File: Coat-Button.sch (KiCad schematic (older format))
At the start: 24 parts, among them IC1 MADW__ATTINY13-MM, P1 CONN_1, P2 CONN_1, P3 CONN_1, P4 CONN_1

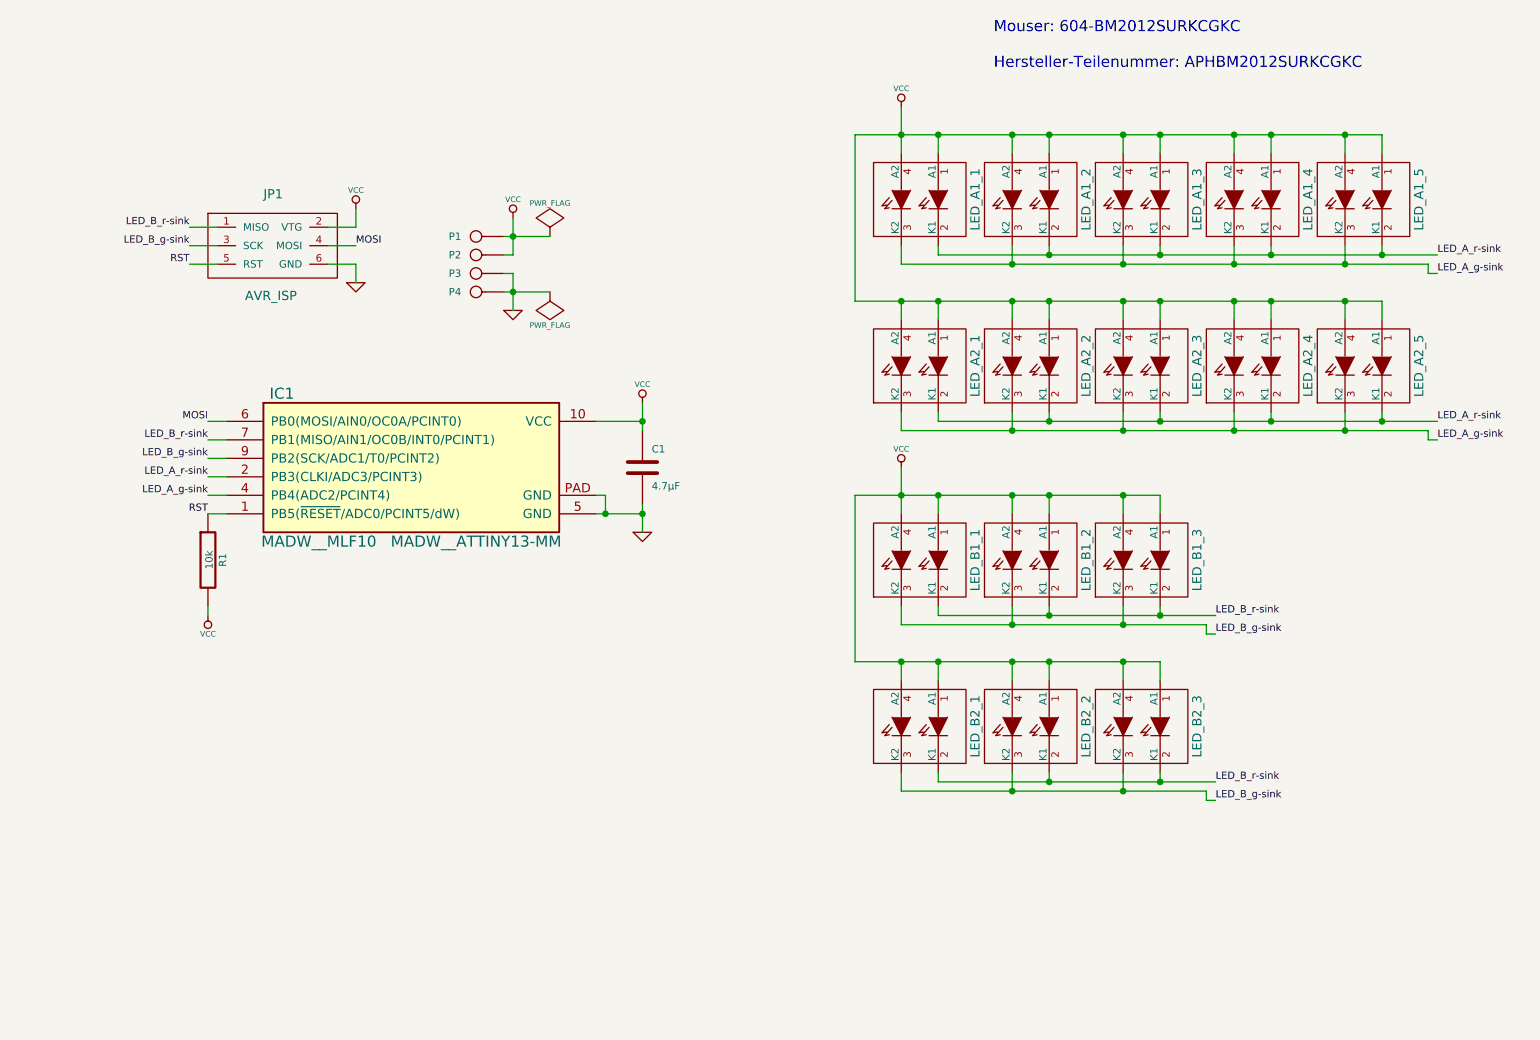
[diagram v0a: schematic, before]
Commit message: On-board ATtiny13 wasn't doable. Not enough space.
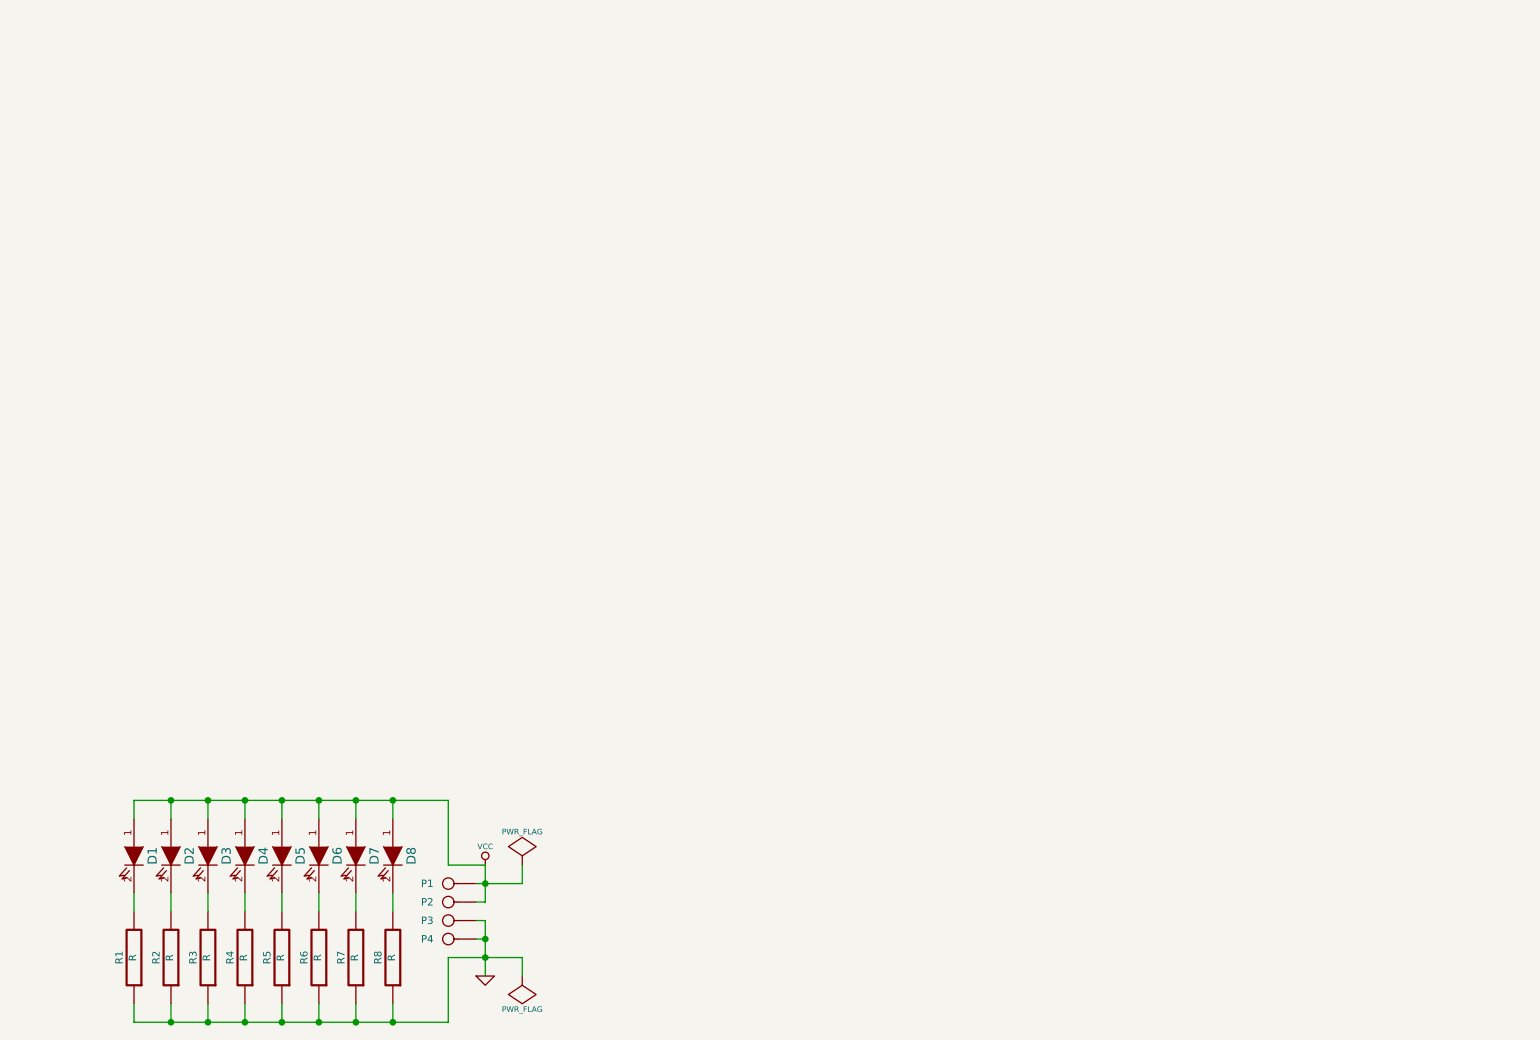
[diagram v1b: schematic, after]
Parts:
- removed C1: 4.7µF, symbol C
- removed IC1: MADW__ATTINY13-MM, MADW__MLF10, symbol MADW__ATTINY13-MM
- removed JP1: AVR_ISP, symbol MADW__AVR_ISP
- removed LED_A1_1, LED_A1_2, LED_A1_3, LED_A1_4, LED_A1_5, LED_A2_1, LED_A2_2, LED_A2_3, LED_A2_4, LED_A2_5, LED_B1_1, LED_B1_2, LED_B1_3, LED_B2_1, LED_B2_2, LED_B2_3: MADW__BI-LED, symbol MADW__BI-LED
- added D1, D2, D3, D4, D5, D6, D7, D8: LED, symbol LED
- added R2, R3, R4, R5, R6, R7, R8: R, symbol R
- R1: value 10k -> R
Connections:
- net RST is gone; now on net GND: R1.1
- net GND: now also R2.1, R3.1, R4.1, R5.1, R6.1, R7.1, R8.1
- net VCC: now also D1.1 (A), D2.1 (A), D3.1 (A), D4.1 (A), D5.1 (A), D6.1 (A), D7.1 (A), D8.1 (A); no longer R1.2
- new net: D1.2 (K), R1.2
- new net: D2.2 (K), R2.2
- new net: D3.2 (K), R3.2
- new net: D4.2 (K), R4.2
- new net: D5.2 (K), R5.2
- new net: D6.2 (K), R6.2
- new net: D7.2 (K), R7.2
- new net: D8.2 (K), R8.2
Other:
- note removed: "Mouser: 604-BM2012SURKCGKC\n\nHersteller-Teilenummer: APHBM2012SURKCGKC\n"

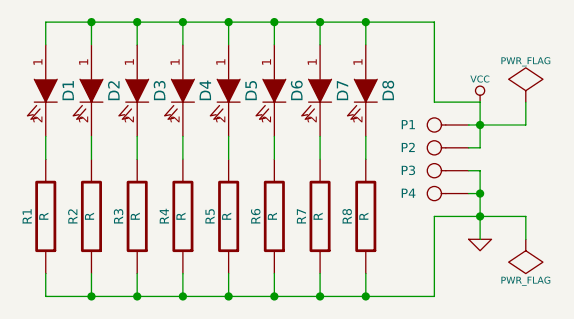
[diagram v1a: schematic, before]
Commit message: Added some stuff to the 'Driver-Board'.
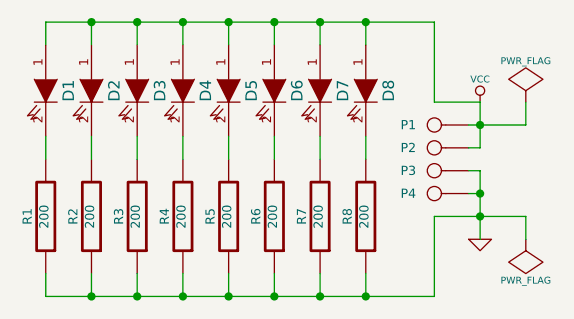
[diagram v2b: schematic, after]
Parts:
- R1, R2, R3, R4, R5, R6, R7, R8: value R -> 200
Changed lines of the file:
@@
 P 2950 5600
 F 0 "R1" V 3030 5600 40  0000 C CNN
-F 1 "R" V 2957 5601 40  0000 C CNN
+F 1 "200" V 2957 5601 40  0000 C CNN
 F 2 "" V 2880 5600 30  0000 C CNN
 F 3 "" H 2950 5600 30  0000 C CNN
@@
 P 3150 5600
 F 0 "R2" V 3230 5600 40  0000 C CNN
-F 1 "R" V 3157 5601 40  0000 C CNN
+F 1 "200" V 3157 5601 40  0000 C CNN
 F 2 "" V 3080 5600 30  0000 C CNN
 F 3 "" H 3150 5600 30  0000 C CNN
@@
 P 3350 5600
 F 0 "R3" V 3430 5600 40  0000 C CNN
-F 1 "R" V 3357 5601 40  0000 C CNN
+F 1 "200" V 3357 5601 40  0000 C CNN
 F 2 "" V 3280 5600 30  0000 C CNN
 F 3 "" H 3350 5600 30  0000 C CNN
@@
 P 3550 5600
 F 0 "R4" V 3630 5600 40  0000 C CNN
-F 1 "R" V 3557 5601 40  0000 C CNN
+F 1 "200" V 3557 5601 40  0000 C CNN
 F 2 "" V 3480 5600 30  0000 C CNN
 F 3 "" H 3550 5600 30  0000 C CNN
@@
 P 3750 5600
 F 0 "R5" V 3830 5600 40  0000 C CNN
-F 1 "R" V 3757 5601 40  0000 C CNN
+F 1 "200" V 3757 5601 40  0000 C CNN
 F 2 "" V 3680 5600 30  0000 C CNN
 F 3 "" H 3750 5600 30  0000 C CNN
@@
 P 3950 5600
 F 0 "R6" V 4030 5600 40  0000 C CNN
-F 1 "R" V 3957 5601 40  0000 C CNN
+F 1 "200" V 3957 5601 40  0000 C CNN
 F 2 "" V 3880 5600 30  0000 C CNN
 F 3 "" H 3950 5600 30  0000 C CNN
@@
 P 4150 5600
 F 0 "R7" V 4230 5600 40  0000 C CNN
-F 1 "R" V 4157 5601 40  0000 C CNN
+F 1 "200" V 4157 5601 40  0000 C CNN
 F 2 "" V 4080 5600 30  0000 C CNN
 F 3 "" H 4150 5600 30  0000 C CNN
@@
 P 4350 5600
 F 0 "R8" V 4430 5600 40  0000 C CNN
-F 1 "R" V 4357 5601 40  0000 C CNN
+F 1 "200" V 4357 5601 40  0000 C CNN
 F 2 "" V 4280 5600 30  0000 C CNN
 F 3 "" H 4350 5600 30  0000 C CNN

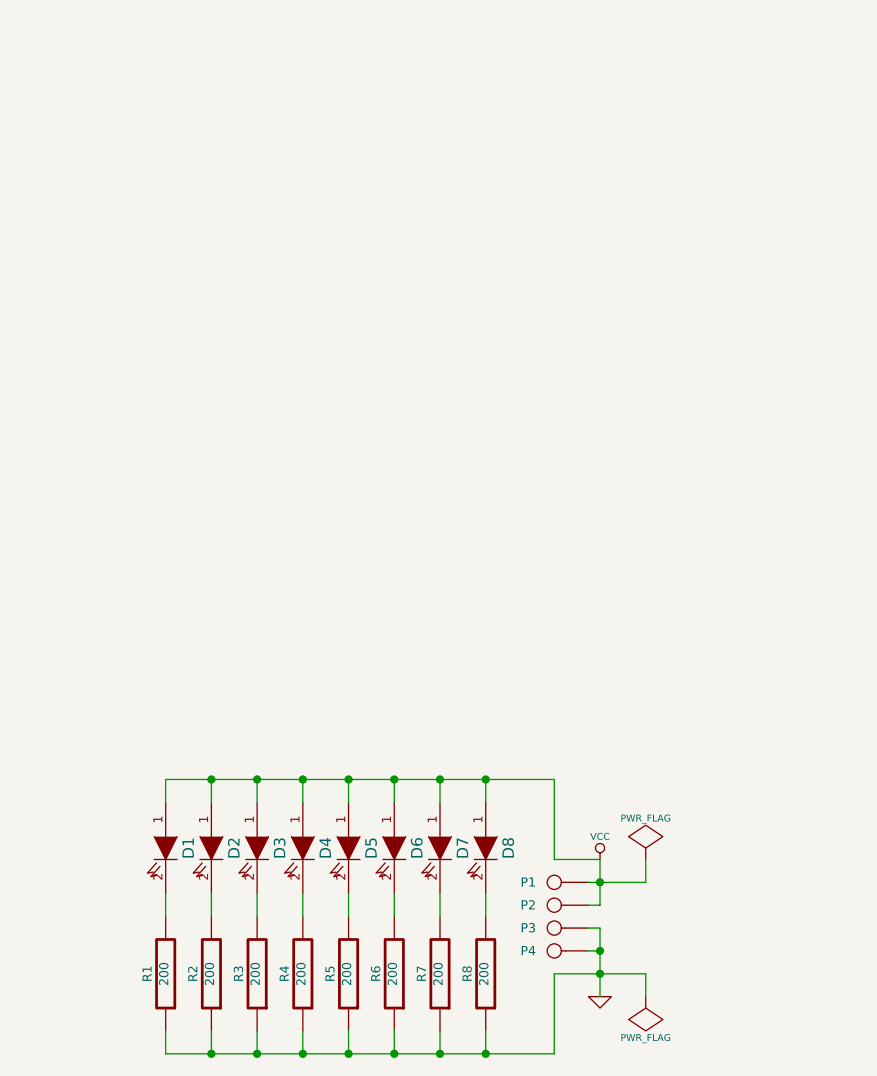
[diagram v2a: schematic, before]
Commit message: Managed to get an ATtiny13 (DFN10) on there again ;-)
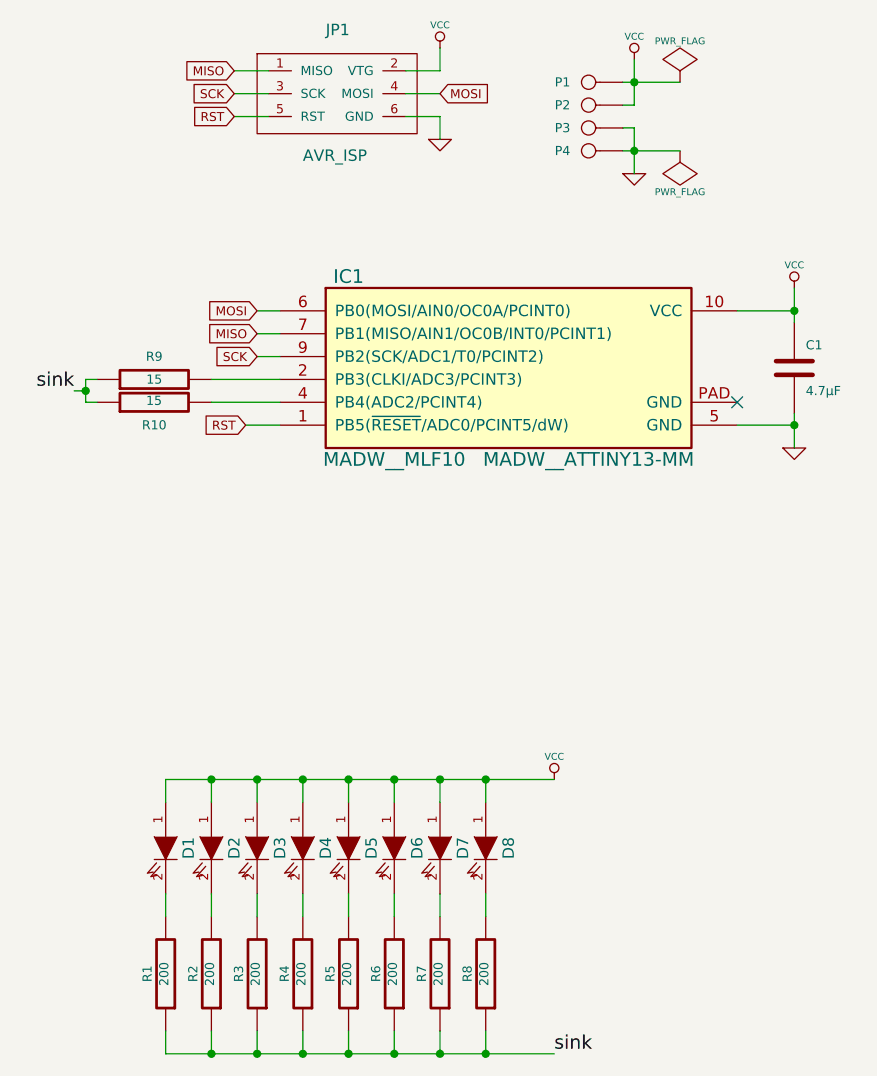
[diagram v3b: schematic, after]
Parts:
- added C1: 4.7µF, symbol C
- added IC1: MADW__ATTINY13-MM, MADW__MLF10, symbol MADW__ATTINY13-MM
- added JP1: AVR_ISP, symbol MADW__AVR_ISP
- added R10, R9: 15, symbol R
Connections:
- net GND: now also C1.2, IC1.5 (GND), JP1.6 (GND); no longer R1.1, R2.1, R3.1, R4.1, R5.1, R6.1, R7.1, R8.1
- net VCC: now also C1.1, IC1.10 (VCC), JP1.2 (VTG)
- new net: IC1.2 (PB3(CLKI/ADC3/PCINT3)), R9.2
- new net: IC1.4 (PB4(ADC2/PCINT4)), R10.2
- new net MISO: IC1.7 (PB1(MISO/AIN1/OC0B/INT0/PCINT1)), JP1.1 (MISO)
- new net MOSI: IC1.6 (PB0(MOSI/AIN0/OC0A/PCINT0)), JP1.4 (MOSI)
- new net RST: IC1.1 (PB5(~RESET~/ADC0/PCINT5/dW)), JP1.5 (RST)
- new net SCK: IC1.9 (PB2(SCK/ADC1/T0/PCINT2)), JP1.3 (SCK)
- new net sink: R1.1, R10.1, R2.1, R3.1, R4.1, R5.1, R6.1, R7.1, R8.1, R9.1
- no-connect marks 0 -> 1
